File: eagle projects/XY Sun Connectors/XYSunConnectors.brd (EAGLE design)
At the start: 25.1 x 25.1 mm, 2 parts

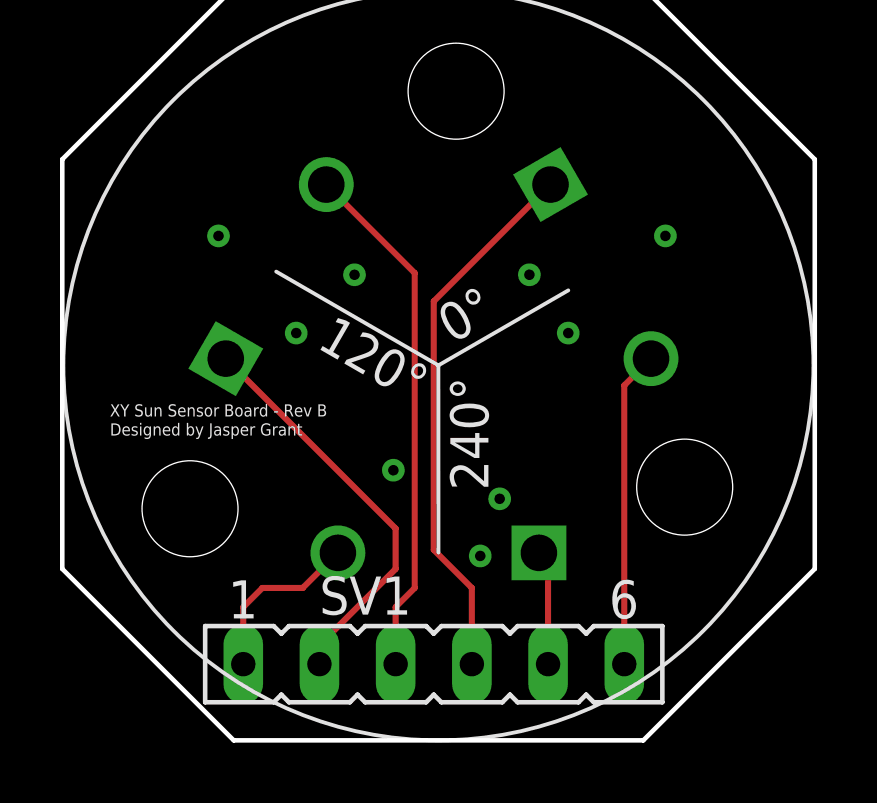
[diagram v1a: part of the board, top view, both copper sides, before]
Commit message: Added proper connectors on XY Sun Connectors
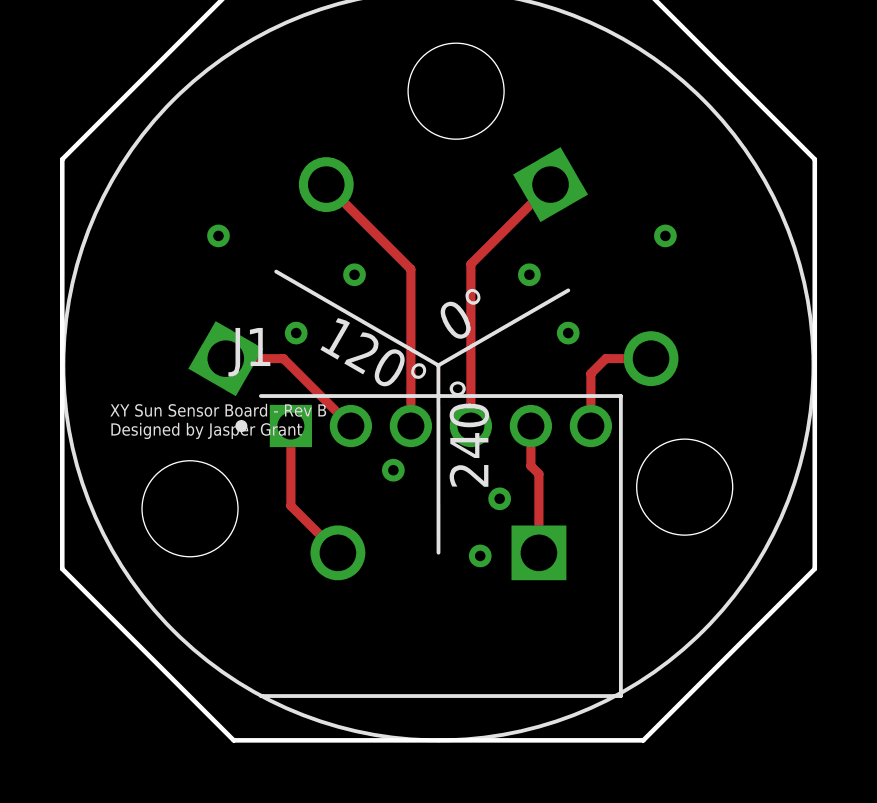
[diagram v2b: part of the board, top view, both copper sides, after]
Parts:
- removed SV1: (no value), con-lsta:FE06
- added J1: 830-10-006-20-005000, 830-10-006-20-005000:830-10-006-20-005000
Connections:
- net A1: now also J1.6; no longer SV1.6
- net A2: now also J1.3; no longer SV1.3
- net A3: now also J1.1; no longer SV1.1
- net C1: now also J1.4; no longer SV1.4
- net C2: now also J1.2; no longer SV1.2
- net C3: now also J1.5; no longer SV1.5
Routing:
- net C1: track 18.1 -> 9.15 mm
- net C2: track 13.6 -> 5.10 mm
- net A2: track 17.5 -> 9.22 mm
- net A1: track 10.6 -> 3.96 mm
- net A3: track 6.44 -> 4.88 mm
- net C3: track 3.84 -> 4.34 mm
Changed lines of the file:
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@@
 </layers>
 <board>
+<fusionsync huburn="a.YnVzaW5lc3M6bXlkYWwxNjA" projecturn="a.YnVzaW5lc3M6bXlkYWwxNjAjRDIwMjEwNTEzNDExOTkzODUx" f3durn="urn:adsk.wipprod:dm.lineage:cc_j59BfRrWnWFQx7fqqxg" pcbguid="" lastpulledtime="" lastsyncedchangeguid="" latestrevisionid="fe8fd6fa-06fe-44e9-a56d-1bd3fea7ef0a" lastsyncedrevisionid="fe8fd6fa-06fe-44e9-a56d-1bd3fea7ef0a" lastboardhashguid="d63d737b-1083-8567-df27-b1f59bee592d" lastpushedtime="2021-10-21T01:29:21Z" linktopcb3d="true"/>
 <plain>
 <wire x1="23.1775" y1="63.5" x2="36.83" y2="63.5" width="0.1524" layer="20"/>
@@
 </autorouter>
 <elements>
-<element name="A2" library="my_library" library_urn="urn:adsk.eagle:library:22876504" package="XY_SUN_SENOR_MASK" value="XY_SUN_SENSOR" x="30" y="76" smashed="yes" rot="R30"/>
-<element name="SV1" library="con-lsta" library_urn="urn:adsk.eagle:library:161" package="FE06" package3d_urn="urn:adsk.eagle:package:8191/1" value="" x="29.845" y="66.04" smashed="yes">
-<attribute name="MF" value="" x="29.845" y="66.04" size="1.778" layer="27" display="off"/>
-<attribute name="MPN" value="" x="29.845" y="66.04" size="1.778" layer="27" display="off"/>
-<attribute name="NAME" x="26.035" y="67.691" size="1.27" layer="25" ratio="10"/>
-<attribute name="OC_FARNELL" value="unknown" x="29.845" y="66.04" size="1.778" layer="27" display="off"/>
-<attribute name="OC_NEWARK" value="unknown" x="29.845" y="66.04" size="1.778" layer="27" display="off"/>
-<attribute name="POPULARITY" value="11" x="29.845" y="66.04" size="1.778" layer="27" display="off"/>
-<attribute name="VALUE" x="22.225" y="63.119" size="1.27" layer="27" ratio="10"/>
+<element name="A2" library="my_library" library_urn="urn:adsk.eagle:library:22876504" package="XY_SUN_SENOR_MASK" override_package3d_urn="urn:adsk.eagle:package:31634060/3" override_package_urn="urn:adsk.eagle:footprint:31634061/1" value="XY_SUN_SENSOR" x="30" y="76" smashed="yes" rot="R30"/>
+<element name="J1" library="830-10-006-20-005000" package="830-10-006-20-005000" override_package3d_urn="urn:adsk.eagle:package:31634800/3" override_package_urn="urn:adsk.eagle:footprint:31634826/1" value="830-10-006-20-005000" x="25.0825" y="73.9775" smashed="yes">
+<attribute name="AVAILABILITY" value="In Stock" x="25.0825" y="73.9775" size="1.778" layer="27" display="off"/>
+<attribute name="COMMENT" value="2355104-4" x="25.0825" y="73.9775" size="1.778" layer="27" display="off"/>
+<attribute name="DESCRIPTION" value=" Pin 4P,2MM,BRK HDR,SRVT,2.8,0.1AU,TB W/CAP 4 POS " x="25.0825" y="73.9775" size="1.778" layer="27" display="off"/>
+<attribute name="MF" value="TE Connectivity" x="25.0825" y="73.9775" size="1.778" layer="27" display="off"/>
+<attribute name="MP" value="2355104-4" x="25.0825" y="73.9775" size="1.778" layer="27" display="off"/>
+<attribute name="NAME" x="23.0825" y="75.9775" size="1.27" layer="25"/>
+<attribute name="PACKAGE" value="None" x="25.0825" y="73.9775" size="1.778" layer="27" display="off"/>
+<attribute name="PRICE" value="None" x="25.0825" y="73.9775" size="1.778" layer="27" display="off"/>
+<attribute name="PURCHASE-URL" value="https://pricing.snapeda.com/search/part/2355104-4/?ref=eda" x="25.0825" y="73.9775" size="1.778" layer="27" display="off"/>
+<attribute name="VALUE" x="23.0825" y="62.9775" size="1.27" layer="27"/>
 </element>
 </elements>
@@
 <signal name="A3">
 <contactref element="A2" pad="A3"/>
-<contactref element="SV1" pad="1"/>
-<wire x1="23.495" y1="65.405" x2="23.495" y2="66.04" width="0" layer="19" extent="1-1"/>
-<wire x1="26.65" y1="69.749996875" x2="25.480003125" y2="68.58" width="0.2032" layer="1"/>
-<wire x1="25.480003125" y1="68.58" x2="24.13" y2="68.58" width="0.2032" layer="1"/>
-<wire x1="24.13" y1="68.58" x2="23.495" y2="67.945" width="0.2032" layer="1"/>
-<wire x1="23.495" y1="67.945" x2="23.495" y2="65.405" width="0.2032" layer="1"/>
+<contactref element="J1" pad="1"/>
+<wire x1="25.0825" y1="73.9775" x2="25.0825" y2="71.317496875" width="0.3048" layer="1"/>
+<wire x1="25.0825" y1="71.317496875" x2="26.65" y2="69.749996875" width="0.3048" layer="1"/>
 </signal>
 <signal name="C3">
 <contactref element="A2" pad="C3"/>
-<contactref element="SV1" pad="5"/>
-<wire x1="33.655" y1="69.44499375" x2="33.349996875" y2="69.749996875" width="0.2032" layer="1"/>
-<wire x1="33.655" y1="66.04" x2="33.655" y2="69.44499375" width="0.2032" layer="1"/>
+<contactref element="J1" pad="5"/>
+<wire x1="33.0825" y1="73.9775" x2="33.0825" y2="72.645" width="0.3048" layer="1"/>
+<wire x1="33.349996875" y1="72.377503125" x2="33.349996875" y2="69.749996875" width="0.3048" layer="1"/>
+<wire x1="33.0825" y1="72.645" x2="33.349996875" y2="72.377503125" width="0.3048" layer="1"/>
 </signal>
 <signal name="C2">
 <contactref element="A2" pad="C2"/>
-<contactref element="SV1" pad="2"/>
-<wire x1="26.035" y1="66.04" x2="26.035" y2="66.675" width="0.2032" layer="1"/>
-<wire x1="26.035" y1="66.675" x2="28.575" y2="69.215" width="0.2032" layer="1"/>
-<wire x1="22.912340625" y1="76.223815625" x2="28.575" y2="70.56115625" width="0.2032" layer="1"/>
-<wire x1="28.575" y1="70.56115625" x2="28.575" y2="69.215" width="0.2032" layer="1"/>
+<contactref element="J1" pad="2"/>
+<wire x1="27.0825" y1="73.9775" x2="24.836184375" y2="76.223815625" width="0.3048" layer="1"/>
+<wire x1="24.836184375" y1="76.223815625" x2="22.912340625" y2="76.223815625" width="0.3048" layer="1"/>
 </signal>
 <signal name="N$7">
@@
 <signal name="C1">
 <contactref element="A2" pad="C1"/>
-<contactref element="SV1" pad="4"/>
-<wire x1="31.115" y1="66.04" x2="31.115" y2="68.58" width="0.2032" layer="1"/>
-<wire x1="31.115" y1="68.58" x2="29.845" y2="69.85" width="0.2032" layer="1"/>
-<wire x1="29.845" y1="69.85" x2="29.845" y2="78.133528125" width="0.2032" layer="1"/>
-<wire x1="29.845" y1="78.133528125" x2="33.73765625" y2="82.026184375" width="0.2032" layer="1"/>
+<contactref element="J1" pad="4"/>
+<wire x1="31.0825" y1="73.9775" x2="31.0825" y2="79.371028125" width="0.3048" layer="1"/>
+<wire x1="31.0825" y1="79.371028125" x2="33.73765625" y2="82.026184375" width="0.3048" layer="1"/>
 </signal>
 <signal name="A2">
 <contactref element="A2" pad="A2"/>
-<contactref element="SV1" pad="3"/>
-<wire x1="28.575" y1="66.04" x2="28.575" y2="67.945" width="0.2032" layer="1"/>
-<wire x1="28.575" y1="67.945" x2="29.21" y2="68.58" width="0.2032" layer="1"/>
-<wire x1="29.21" y1="79.078521875" x2="26.2623375" y2="82.026184375" width="0.2032" layer="1"/>
-<wire x1="29.21" y1="68.58" x2="29.21" y2="79.078521875" width="0.2032" layer="1"/>
+<contactref element="J1" pad="3"/>
+<wire x1="29.0825" y1="73.9775" x2="29.0825" y2="79.206021875" width="0.3048" layer="1"/>
+<wire x1="29.0825" y1="79.206021875" x2="26.2623375" y2="82.026184375" width="0.3048" layer="1"/>
 </signal>
 <signal name="A1">
 <contactref element="A2" pad="A1"/>
-<contactref element="SV1" pad="6"/>
-<wire x1="36.195" y1="66.04" x2="36.195" y2="75.33115625" width="0.2032" layer="1"/>
-<wire x1="36.195" y1="75.33115625" x2="37.08765625" y2="76.2238125" width="0.2032" layer="1"/>
+<contactref element="J1" pad="6"/>
+<wire x1="35.0825" y1="73.9775" x2="35.0825" y2="75.7225" width="0.3048" layer="1"/>
+<wire x1="35.5838125" y1="76.2238125" x2="37.08765625" y2="76.2238125" width="0.3048" layer="1"/>
+<wire x1="35.0825" y1="75.7225" x2="35.5838125" y2="76.2238125" width="0.3048" layer="1"/>
 </signal>
 </signals>
@@
 </note>
 <note version="8.3" severity="warning">
-Since Version 8.3, EAGLE supports URNs for individual library
-assets (packages, symbols, and devices). The URNs of those assets
-will not be understood (or retained) with this version.
+Since Version 8.3, EAGLE supports Fusion synchronisation.
+This feature will not be available in this version and saving
+the document will break the link to the Fusion PCB feature.
 </note>
 <note version="8.3" severity="warning">
@@
 packages will not be understood (or retained) with this version.
 </note>
+<note version="9.4" severity="warning">
+Since Version 9.4, EAGLE supports the overriding of 3D packages
+in schematics and board files. Those overridden 3d packages
+will not be understood (or retained) with this version.
+</note>
 </compatibility>
